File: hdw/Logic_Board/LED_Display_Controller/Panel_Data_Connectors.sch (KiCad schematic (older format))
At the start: 16 parts, among them J2901 STRING 1, J2902 STRING 2, J2903 STRING 3, J2904 STRING 4

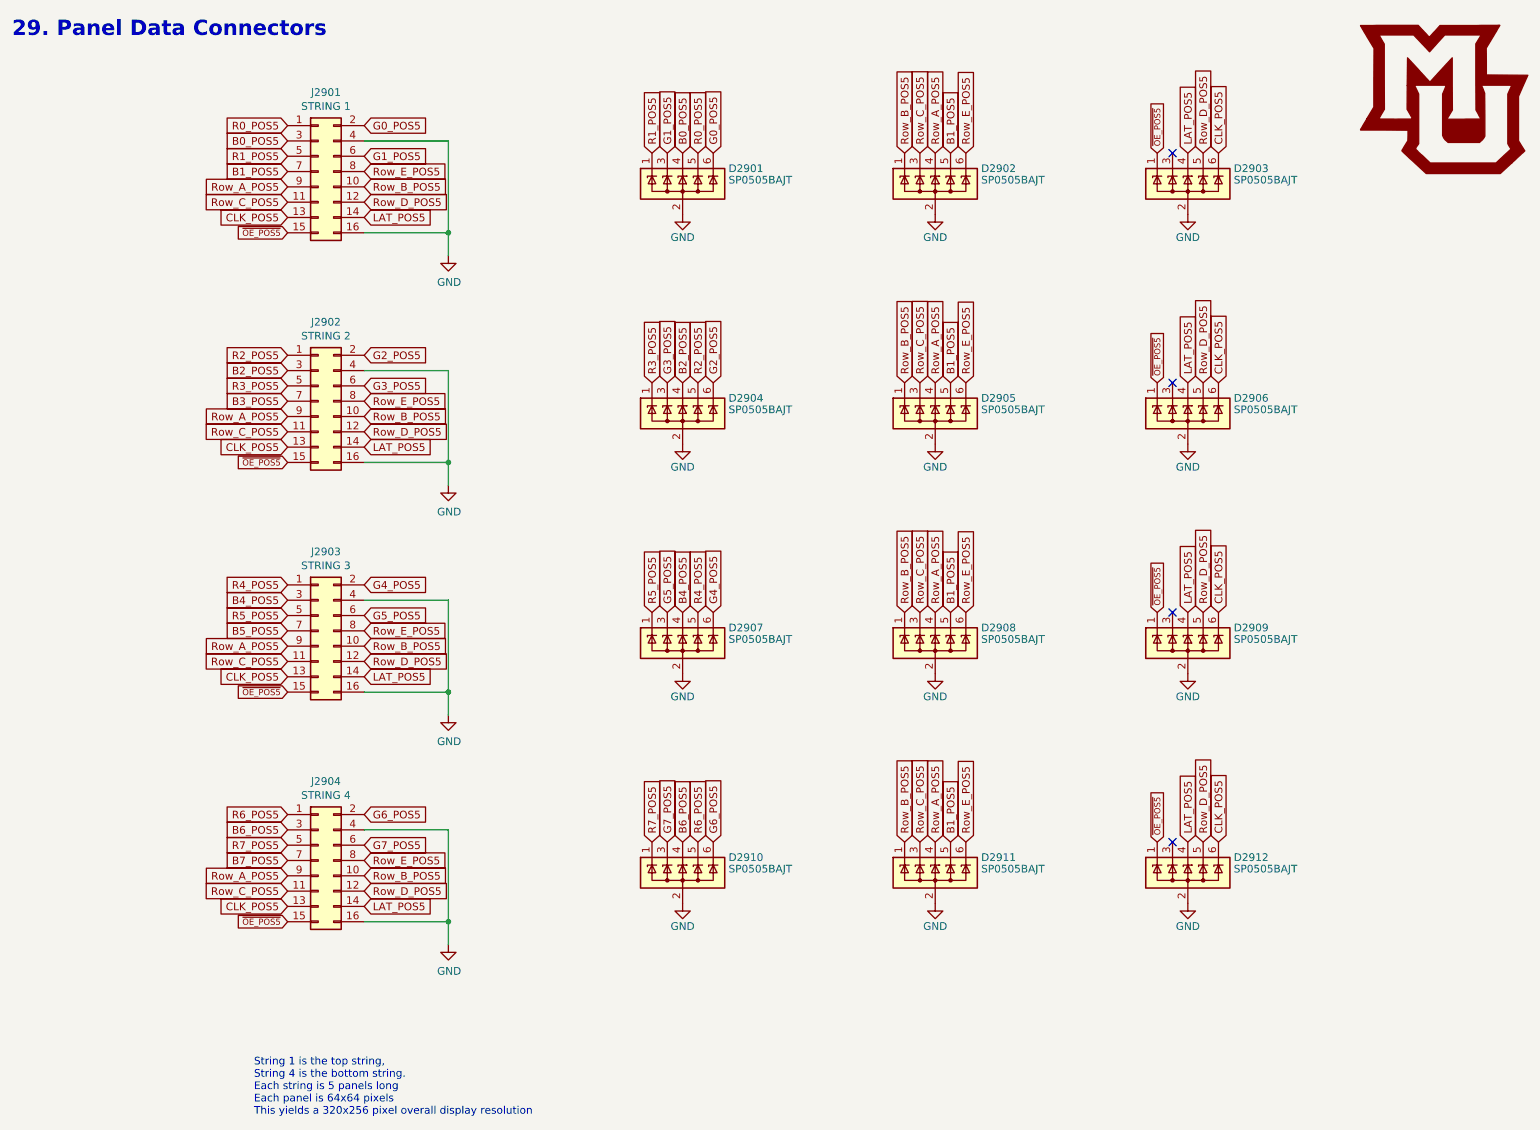
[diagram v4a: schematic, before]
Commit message: Fixed net placement on level shifters, lots of part placements on PCB
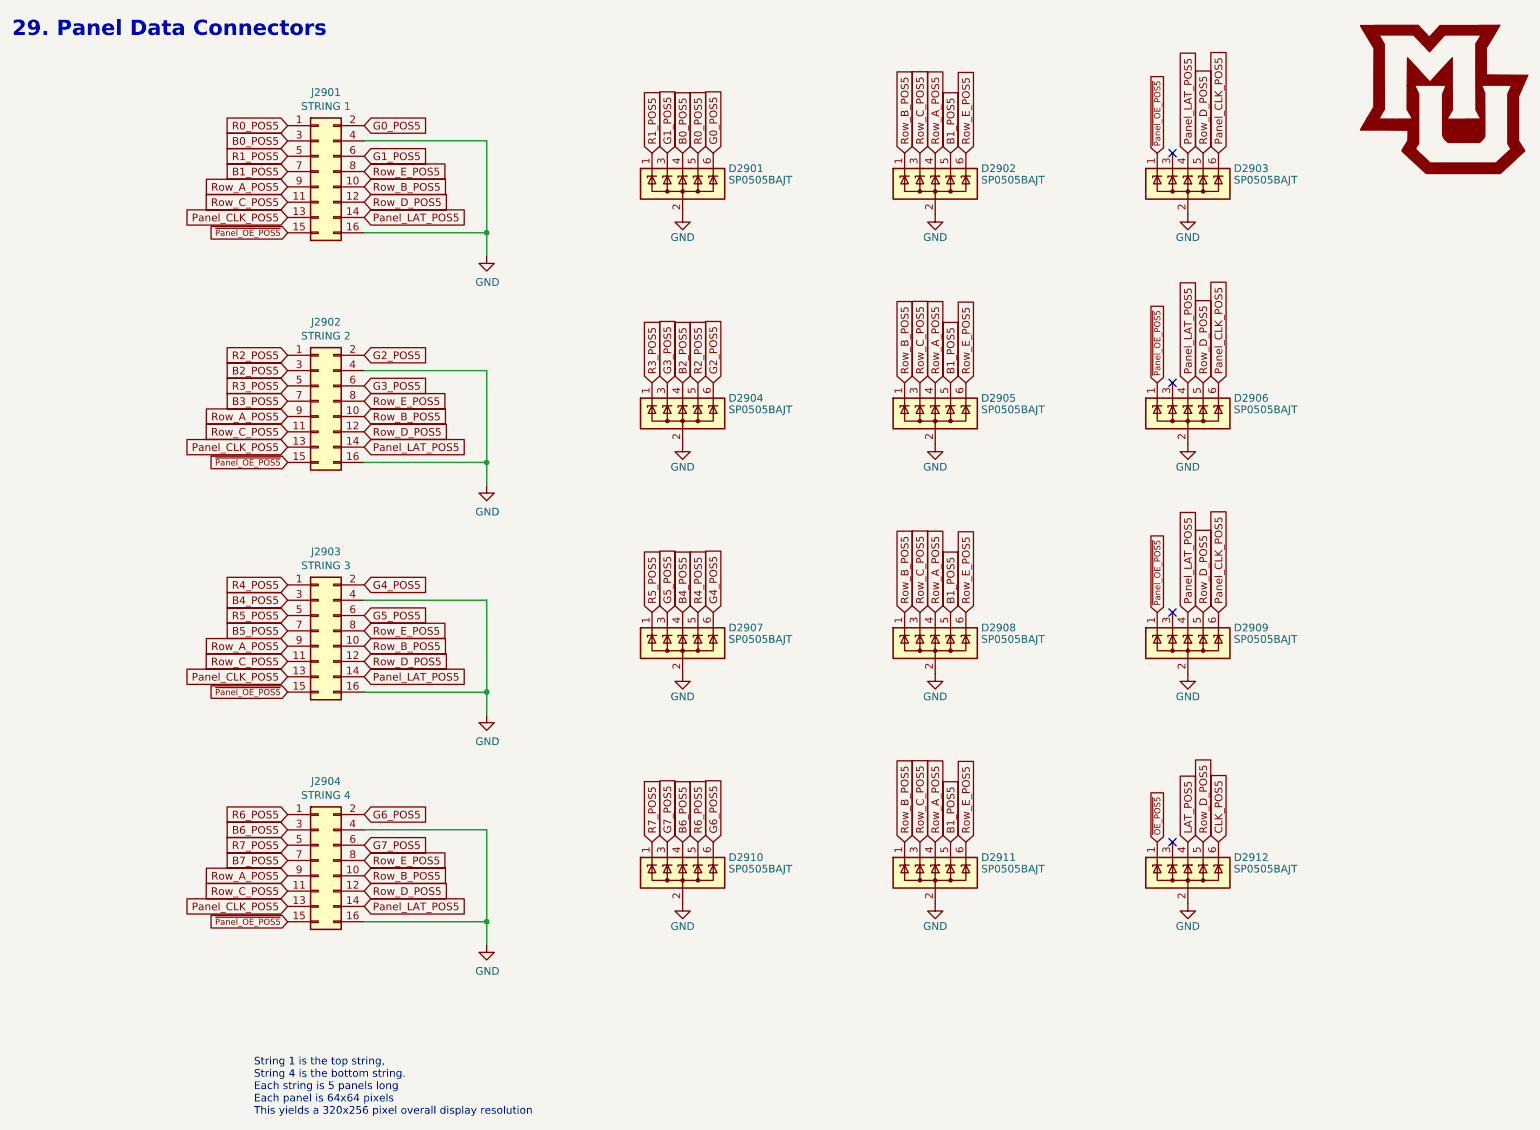
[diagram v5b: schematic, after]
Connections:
- net CLK_POS5: no longer D2903.6 (K), D2906.6 (K), D2909.6 (K), J2901.13 (Pin_13), J2902.13 (Pin_13), J2903.13 (Pin_13), J2904.13 (Pin_13)
- net LAT_POS5: no longer D2903.4 (K), D2906.4 (K), D2909.4 (K), J2901.14 (Pin_14), J2902.14 (Pin_14), J2903.14 (Pin_14), J2904.14 (Pin_14)
- net ~OE_POS5: no longer D2903.1 (K), D2906.1 (K), D2909.1 (K), J2901.15 (Pin_15), J2902.15 (Pin_15), J2903.15 (Pin_15), J2904.15 (Pin_15)
- new net Panel_CLK_POS5: D2903.6 (K), D2906.6 (K), D2909.6 (K), J2901.13 (Pin_13), J2902.13 (Pin_13), J2903.13 (Pin_13), J2904.13 (Pin_13)
- new net Panel_LAT_POS5: D2903.4 (K), D2906.4 (K), D2909.4 (K), J2901.14 (Pin_14), J2902.14 (Pin_14), J2903.14 (Pin_14), J2904.14 (Pin_14)
- new net ~Panel_OE_POS5: D2903.1 (K), D2906.1 (K), D2909.1 (K), J2901.15 (Pin_15), J2902.15 (Pin_15), J2903.15 (Pin_15), J2904.15 (Pin_15)
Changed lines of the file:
@@
 Row_C_POS5
 Text GLabel 2350 1870 0    50   Input ~ 0
-CLK_POS5
+Panel_CLK_POS5
 Text GLabel 2350 1970 0    40   Input ~ 0
-~OE_POS5
+~Panel_OE_POS5
 Text GLabel 2850 1870 2    50   Input ~ 0
-LAT_POS5
+Panel_LAT_POS5
 Text GLabel 2350 1270 0    50   Input ~ 0
 R0_POS5
@@
 L power:GND #PWR02901
 U 1 1 5BB40845
-P 3400 2120
-F 0 "#PWR02901" H 3400 1870 50  0001 C CNN
-F 1 "GND" H 3405 1947 50  0000 C CNN
-F 2 "" H 3400 2120 50  0001 C CNN
-F 3 "" H 3400 2120 50  0001 C CNN
-	1    3400 2120
-	1    0    0    -1
-$EndComp
-Wire Wire Line
-	3400 2120 3400 1970
-Wire Wire Line
-	3400 1970 2850 1970
-Wire Wire Line
-	2850 1370 3400 1370
-Wire Wire Line
-	3400 1370 3400 1970
-Connection ~ 3400 1970
+P 3650 2120
+F 0 "#PWR02901" H 3650 1870 50  0001 C CNN
+F 1 "GND" H 3655 1947 50  0000 C CNN
+F 2 "" H 3650 2120 50  0001 C CNN
+F 3 "" H 3650 2120 50  0001 C CNN
+	1    3650 2120
+	1    0    0    -1
+$EndComp
+Wire Wire Line
+	3650 2120 3650 1970
+Wire Wire Line
+	3650 1370 3650 1970
+Connection ~ 3650 1970
 $Comp
 L Connector_Generic:Conn_02x08_Odd_Even J2902
@@
 Row_C_POS5
 Text GLabel 2350 3370 0    50   Input ~ 0
-CLK_POS5
+Panel_CLK_POS5
 Text GLabel 2350 3470 0    40   Input ~ 0
-~OE_POS5
+~Panel_OE_POS5
 Text GLabel 2850 3370 2    50   Input ~ 0
-LAT_POS5
+Panel_LAT_POS5
 Text GLabel 2350 2770 0    50   Input ~ 0
 R2_POS5
@@
 G3_POS5
 $Comp
-L power:GND #PWR02902
-U 1 1 5BB40C3C
-P 3400 3620
-F 0 "#PWR02902" H 3400 3370 50  0001 C CNN
-F 1 "GND" H 3405 3447 50  0000 C CNN
-F 2 "" H 3400 3620 50  0001 C CNN
-F 3 "" H 3400 3620 50  0001 C CNN
-	1    3400 3620
-	1    0    0    -1
-$EndComp
-Wire Wire Line
-	3400 3620 3400 3470
-Wire Wire Line
-	3400 3470 2850 3470
-Wire Wire Line
-	2850 2870 3400 2870
-Wire Wire Line
-	3400 2870 3400 3470
-Connection ~ 3400 3470
-$Comp
 L Connector_Generic:Conn_02x08_Odd_Even J2903
 U 1 1 5BB40D11
@@
 Row_C_POS5
 Text GLabel 2350 4870 0    50   Input ~ 0
-CLK_POS5
+Panel_CLK_POS5
 Text GLabel 2350 4970 0    40   Input ~ 0
-~OE_POS5
+~Panel_OE_POS5
 Text GLabel 2850 4870 2    50   Input ~ 0
-LAT_POS5
+Panel_LAT_POS5
 Text GLabel 2350 4270 0    50   Input ~ 0
 R4_POS5
@@
 G5_POS5
 $Comp
-L power:GND #PWR02903
-U 1 1 5BB40D26
-P 3400 5120
-F 0 "#PWR02903" H 3400 4870 50  0001 C CNN
-F 1 "GND" H 3405 4947 50  0000 C CNN
-F 2 "" H 3400 5120 50  0001 C CNN
-F 3 "" H 3400 5120 50  0001 C CNN
-	1    3400 5120
-	1    0    0    -1
-$EndComp
-Wire Wire Line
-	3400 5120 3400 4970
-Wire Wire Line
-	3400 4970 2850 4970
-Wire Wire Line
-	2850 4370 3400 4370
-Wire Wire Line
-	3400 4370 3400 4970
-Connection ~ 3400 4970
-$Comp
 L Connector_Generic:Conn_02x08_Odd_Even J2904
 U 1 1 5BB40D31
@@
 Row_C_POS5
 Text GLabel 2350 6370 0    50   Input ~ 0
-CLK_POS5
+Panel_CLK_POS5
 Text GLabel 2350 6470 0    40   Input ~ 0
-~OE_POS5
+~Panel_OE_POS5
 Text GLabel 2850 6370 2    50   Input ~ 0
-LAT_POS5
+Panel_LAT_POS5
 Text GLabel 2350 5770 0    50   Input ~ 0
 R6_POS5
@@
 Text GLabel 2850 5970 2    50   Input ~ 0
 G7_POS5
-$Comp
-L power:GND #PWR02904
-U 1 1 5BB40D46
-P 3400 6620
-F 0 "#PWR02904" H 3400 6370 50  0001 C CNN
-F 1 "GND" H 3405 6447 50  0000 C CNN
-F 2 "" H 3400 6620 50  0001 C CNN
-F 3 "" H 3400 6620 50  0001 C CNN
-	1    3400 6620
-	1    0    0    -1
-$EndComp
-Wire Wire Line
-	3400 6620 3400 6470
-Wire Wire Line
-	3400 6470 2850 6470
-Wire Wire Line
-	2850 5870 3400 5870
-Wire Wire Line
-	3400 5870 3400 6470
-Connection ~ 3400 6470
 Text GLabel 6580 1450 1    50   Input ~ 0
 Row_A_POS5
@@
 B1_POS5
 Text GLabel 8430 1450 1    50   Input ~ 0
-CLK_POS5
+Panel_CLK_POS5
 Text GLabel 8030 1450 1    40   Input ~ 0
-~OE_POS5
+~Panel_OE_POS5
 Text GLabel 6380 1450 1    50   Input ~ 0
 Row_B_POS5
@@
 Row_E_POS5
 Text GLabel 8230 1450 1    50   Input ~ 0
-LAT_POS5
+Panel_LAT_POS5
 Text GLabel 5130 1450 1    50   Input ~ 0
 G0_POS5
@@
 Row_E_POS5
 Text GLabel 8430 2950 1    50   Input ~ 0
-CLK_POS5
+Panel_CLK_POS5
 Text GLabel 8030 2950 1    40   Input ~ 0
-~OE_POS5
+~Panel_OE_POS5
 Text GLabel 8330 2950 1    50   Input ~ 0
 Row_D_POS5
 Text GLabel 8230 2950 1    50   Input ~ 0
-LAT_POS5
+Panel_LAT_POS5
 Text GLabel 8430 4450 1    50   Input ~ 0
-CLK_POS5
+Panel_CLK_POS5
 Text GLabel 8030 4450 1    40   Input ~ 0
-~OE_POS5
+~Panel_OE_POS5
 Text GLabel 8330 4450 1    50   Input ~ 0
 Row_D_POS5
 Text GLabel 8230 4450 1    50   Input ~ 0
-LAT_POS5
+Panel_LAT_POS5
 Text GLabel 8430 5950 1    50   Input ~ 0
 CLK_POS5
@@
 Text GLabel 8230 5950 1    50   Input ~ 0
 LAT_POS5
+Wire Wire Line
+	2850 1970 3650 1970
+Wire Wire Line
+	2850 1370 3650 1370
+$Comp
+L power:GND #PWR0110
+U 1 1 5C1900F3
+P 3650 3620
+F 0 "#PWR0110" H 3650 3370 50  0001 C CNN
+F 1 "GND" H 3655 3447 50  0000 C CNN
+F 2 "" H 3650 3620 50  0001 C CNN
+F 3 "" H 3650 3620 50  0001 C CNN
+	1    3650 3620
+	1    0    0    -1
+$EndComp
+Wire Wire Line
+	3650 3620 3650 3470
+Wire Wire Line
+	3650 2870 3650 3470
+Connection ~ 3650 3470
+Wire Wire Line
+	2850 3470 3650 3470
+Wire Wire Line
+	2850 2870 3650 2870
+$Comp
+L power:GND #PWR0111
+U 1 1 5C190162
+P 3650 5120
+F 0 "#PWR0111" H 3650 4870 50  0001 C CNN
+F 1 "GND" H 3655 4947 50  0000 C CNN
+F 2 "" H 3650 5120 50  0001 C CNN
+F 3 "" H 3650 5120 50  0001 C CNN
+	1    3650 5120
+	1    0    0    -1
+$EndComp
+Wire Wire Line
+	3650 5120 3650 4970
+Wire Wire Line
+	3650 4370 3650 4970
+Connection ~ 3650 4970
+Wire Wire Line
+	2850 4970 3650 4970
+Wire Wire Line
+	2850 4370 3650 4370
+$Comp
+L power:GND #PWR0112
+U 1 1 5C1901F7
+P 3650 6620
+F 0 "#PWR0112" H 3650 6370 50  0001 C CNN
+F 1 "GND" H 3655 6447 50  0000 C CNN
+F 2 "" H 3650 6620 50  0001 C CNN
+F 3 "" H 3650 6620 50  0001 C CNN
+	1    3650 6620
+	1    0    0    -1
+$EndComp
+Wire Wire Line
+	3650 6620 3650 6470
+Wire Wire Line
+	3650 5870 3650 6470
+Connection ~ 3650 6470
+Wire Wire Line
+	2850 6470 3650 6470
+Wire Wire Line
+	2850 5870 3650 5870
 $EndSCHEMATC
